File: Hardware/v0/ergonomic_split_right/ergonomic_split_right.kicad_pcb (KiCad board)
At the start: 2 copper layers, 183 x 172.8 mm, 66 parts, among them J2 Left_Interface, SW1 R50, SW10 R31, SW11 R45, SW12 R51, SW13 R02, SW14 R12, SW15 R22, SW16 R32, SW17 R42, SW18 R54, SW19 R03, SW2 R06, SW20 R13, SW21 R23, SW22 R33, SW23 R43, SW24 R53, SW25 R04, SW26 R14, SW27 R24, SW28 R34, SW29 R44, SW3 R16, SW30 R46, SW31 R05, SW32 R15, SW33 R25, SW34 R35, SW35 R55, SW36 R10, SW37 R30, SW39 R00, SW4 R26, SW40 L_Encoder, SW5 R36, SW6 R52, SW7 R01, SW8 R11, SW9 R21, U2 PCAL9555AHF, U9 TCR2EF33

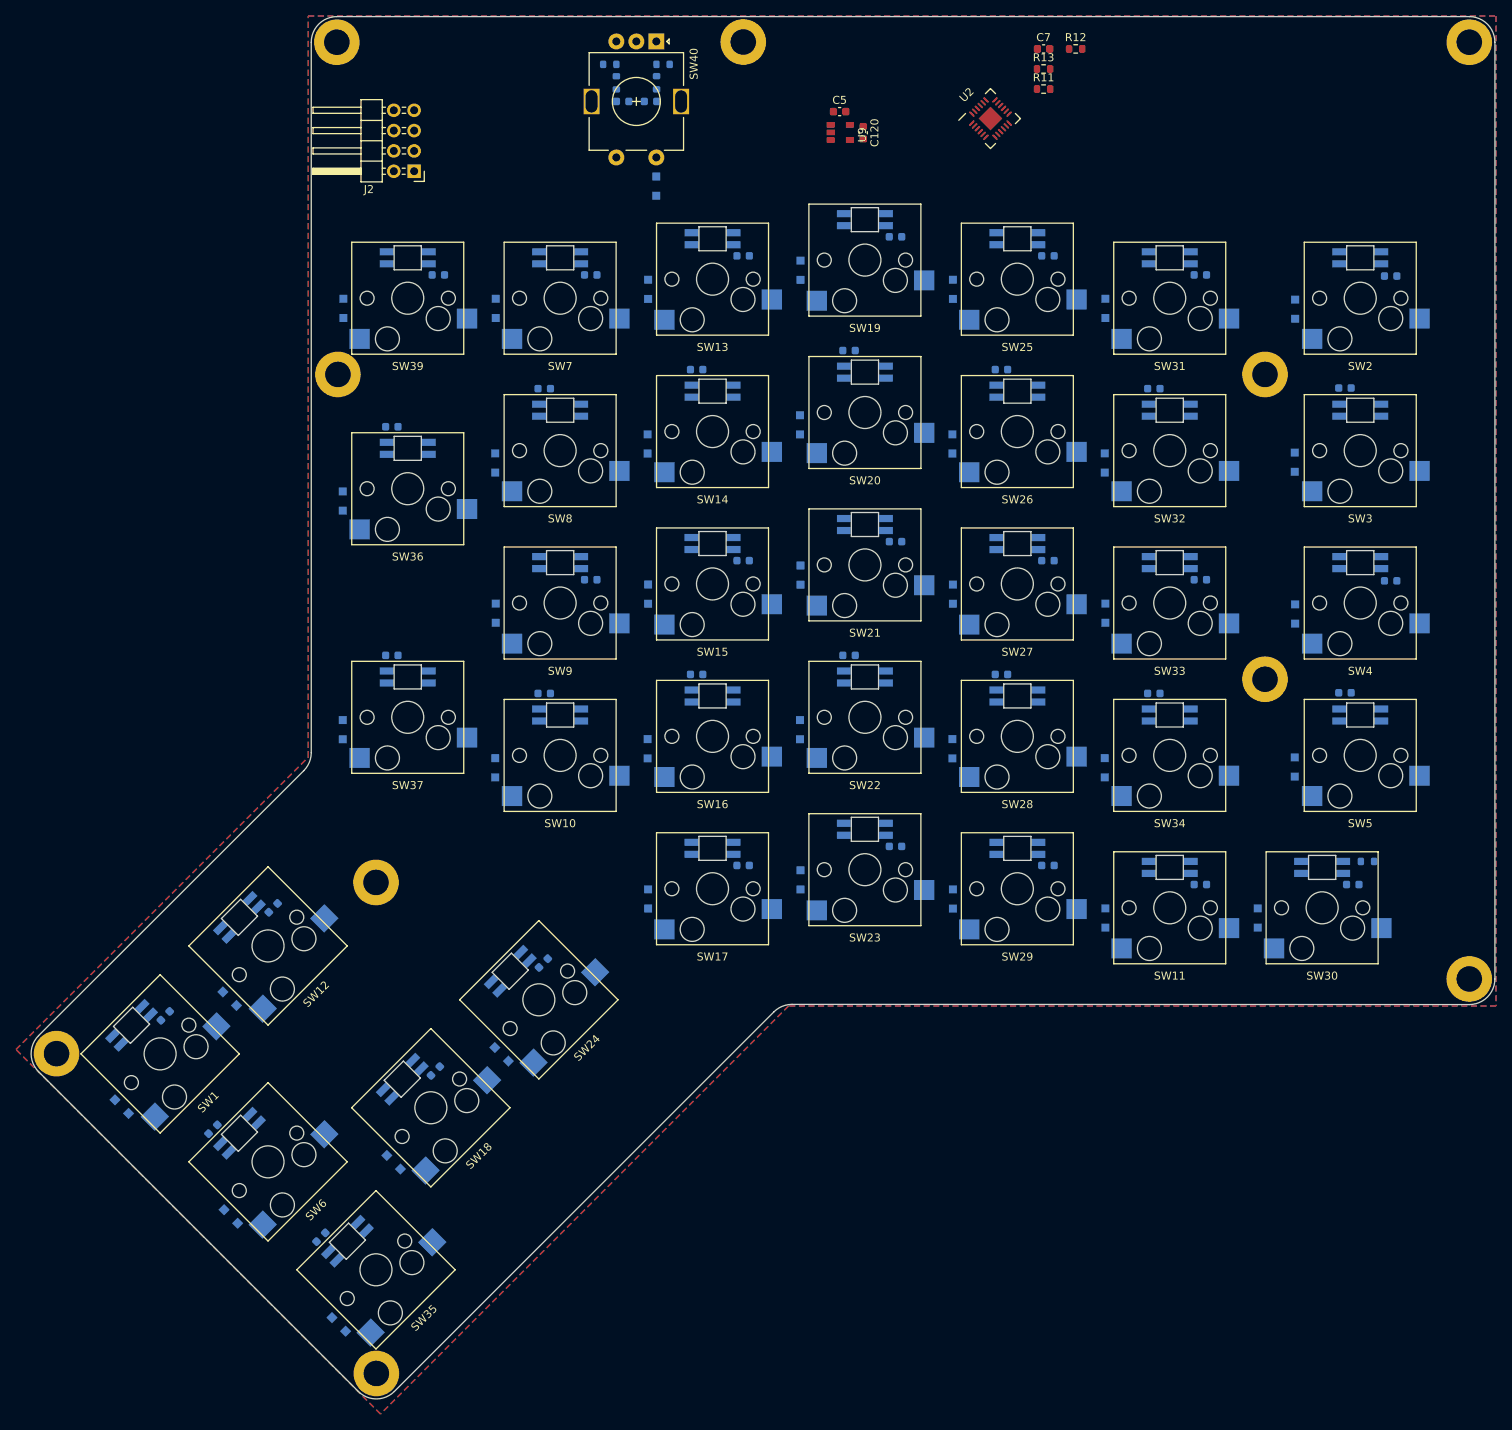
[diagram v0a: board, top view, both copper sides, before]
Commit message: Right side prelim routing mostly done
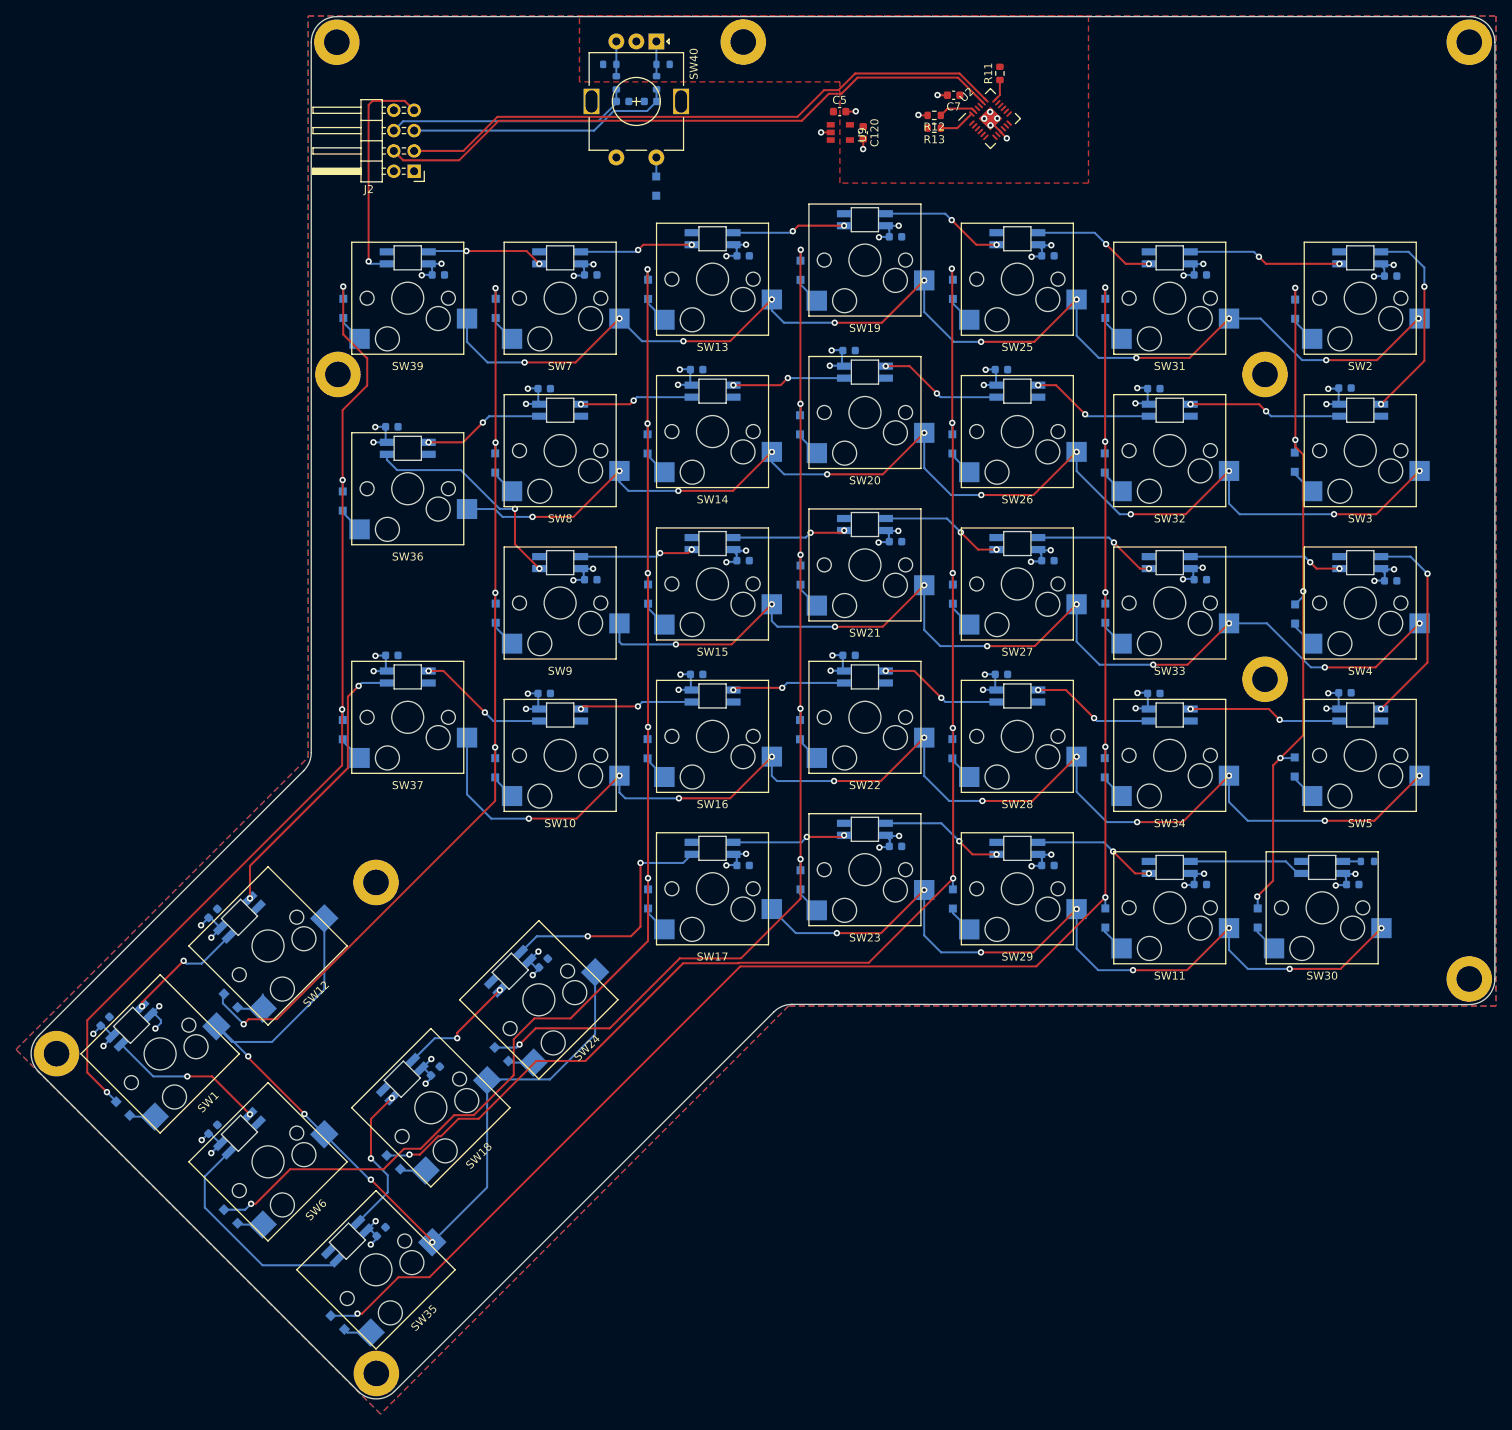
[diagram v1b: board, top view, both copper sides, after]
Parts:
- SW1, SW12: footprint custom_footprint_library:CherryMX_1.00u_KailhSocket_Integrated_Reversed -> custom_footprint_library:CherryMX_1.00u_KailhSocket_Integrated
- SW35: footprint custom_footprint_library:CherryMX_1.00u_KailhSocket_Integrated -> custom_footprint_library:CherryMX_1.00u_KailhSocket_Integrated_Reversed
- SW40: value L_Encoder -> R_Encoder
- moved R12 19.5 mm to (218.2, 50.2), turned to 180 degrees
- moved R13 15.5 mm to (218.2, 51.8), turned to 180 degrees
- moved C7 12.6 mm to (220.6, 47.7), turned to 180 degrees
- moved R11 5.80 mm to (226.4, 44.9), turned to 90 degrees
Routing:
- net /IO Expander/COL[5]: track 0.00 -> 201.8 mm, vias 0 -> 6
- net +5V: track 0.00 -> 175.1 mm, vias 0 -> 76
- net /IO Expander/COL[4]: track 0.00 -> 168.5 mm, vias 0 -> 6
- net /IO Expander/ROW[3]: track 0.00 -> 162.4 mm, vias 0 -> 12
- net /IO Expander/COL[2]: track 0.00 -> 160.6 mm, vias 0 -> 6
- net /IO Expander/ROW[0]: track 0.00 -> 152.4 mm, vias 0 -> 12
- net /IO Expander/ROW[1]: track 0.00 -> 151.5 mm, vias 0 -> 12
- net /IO Expander/COL[3]: track 0.00 -> 134.1 mm, vias 0 -> 6
- net /IO Expander/ROW[2]: track 0.00 -> 130.3 mm, vias 0 -> 10
- net /IO Expander/COL[0]: track 0.00 -> 123.2 mm, vias 0 -> 4
- net /IO Expander/COL[1]: track 0.00 -> 117.6 mm, vias 0 -> 5
- net /IO Expander/ROW[5]: track 0.00 -> 111.0 mm, vias 0 -> 4
- net /IO Expander/ROW[4]: track 0.00 -> 102.5 mm, vias 0 -> 8
- net /IO Expander/COL[6]: track 0.00 -> 87.4 mm, vias 0 -> 5
- net /IO Expander/SCL: track 0.00 -> 79.7 mm
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- added copper zone on F.Cu, net +3V3

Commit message: prelim routing done
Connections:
- D1 pad 1: /IO Expander/COL[6] -> /IO Expander/COL[2]
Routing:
- net /IO Expander/ROW[5]: track 111.0 -> 258.7 mm, vias 4 -> 7
- net /IO Expander/COL[0]: track 123.2 -> 225.4 mm, vias 4 -> 7
- net /IO Expander/ROW[4]: track 102.5 -> 200.6 mm, vias 8 -> 10
- net /IO Expander/COL[1]: track 117.6 -> 203.5 mm, vias 5 -> 8
- net /IO Expander/ROW[3]: track 162.4 -> 242.0 mm, vias 12 -> 14
- net /IO Expander/COL[2]: track 160.6 -> 226.4 mm, vias 6 -> 9
- net /IO Expander/COL[3]: track 134.1 -> 196.7 mm, vias 6 -> 7
- net /IO Expander/ROW[2]: track 130.3 -> 190.1 mm, vias 10 -> 12
- net /IO Expander/ROW[6]: track 0.00 -> 57.8 mm, vias 0 -> 2
- net /IO Expander/COL[6]: track 87.4 -> 140.7 mm, vias 5 -> 6
- net /IO Expander/COL[4]: track 168.5 -> 214.2 mm, vias 6 -> 7
- net /IO Expander/ROW[1]: track 151.5 -> 192.9 mm, vias 12 -> 14
- net /IO Expander/COL[5]: track 201.8 -> 232.9 mm, vias 6 -> 7
- net /IO Expander/ROW[0]: track 152.4 -> 174.7 mm, vias 12 -> 14
- net +3V3: track 0.00 -> 2.36 mm, vias 0 -> 2
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
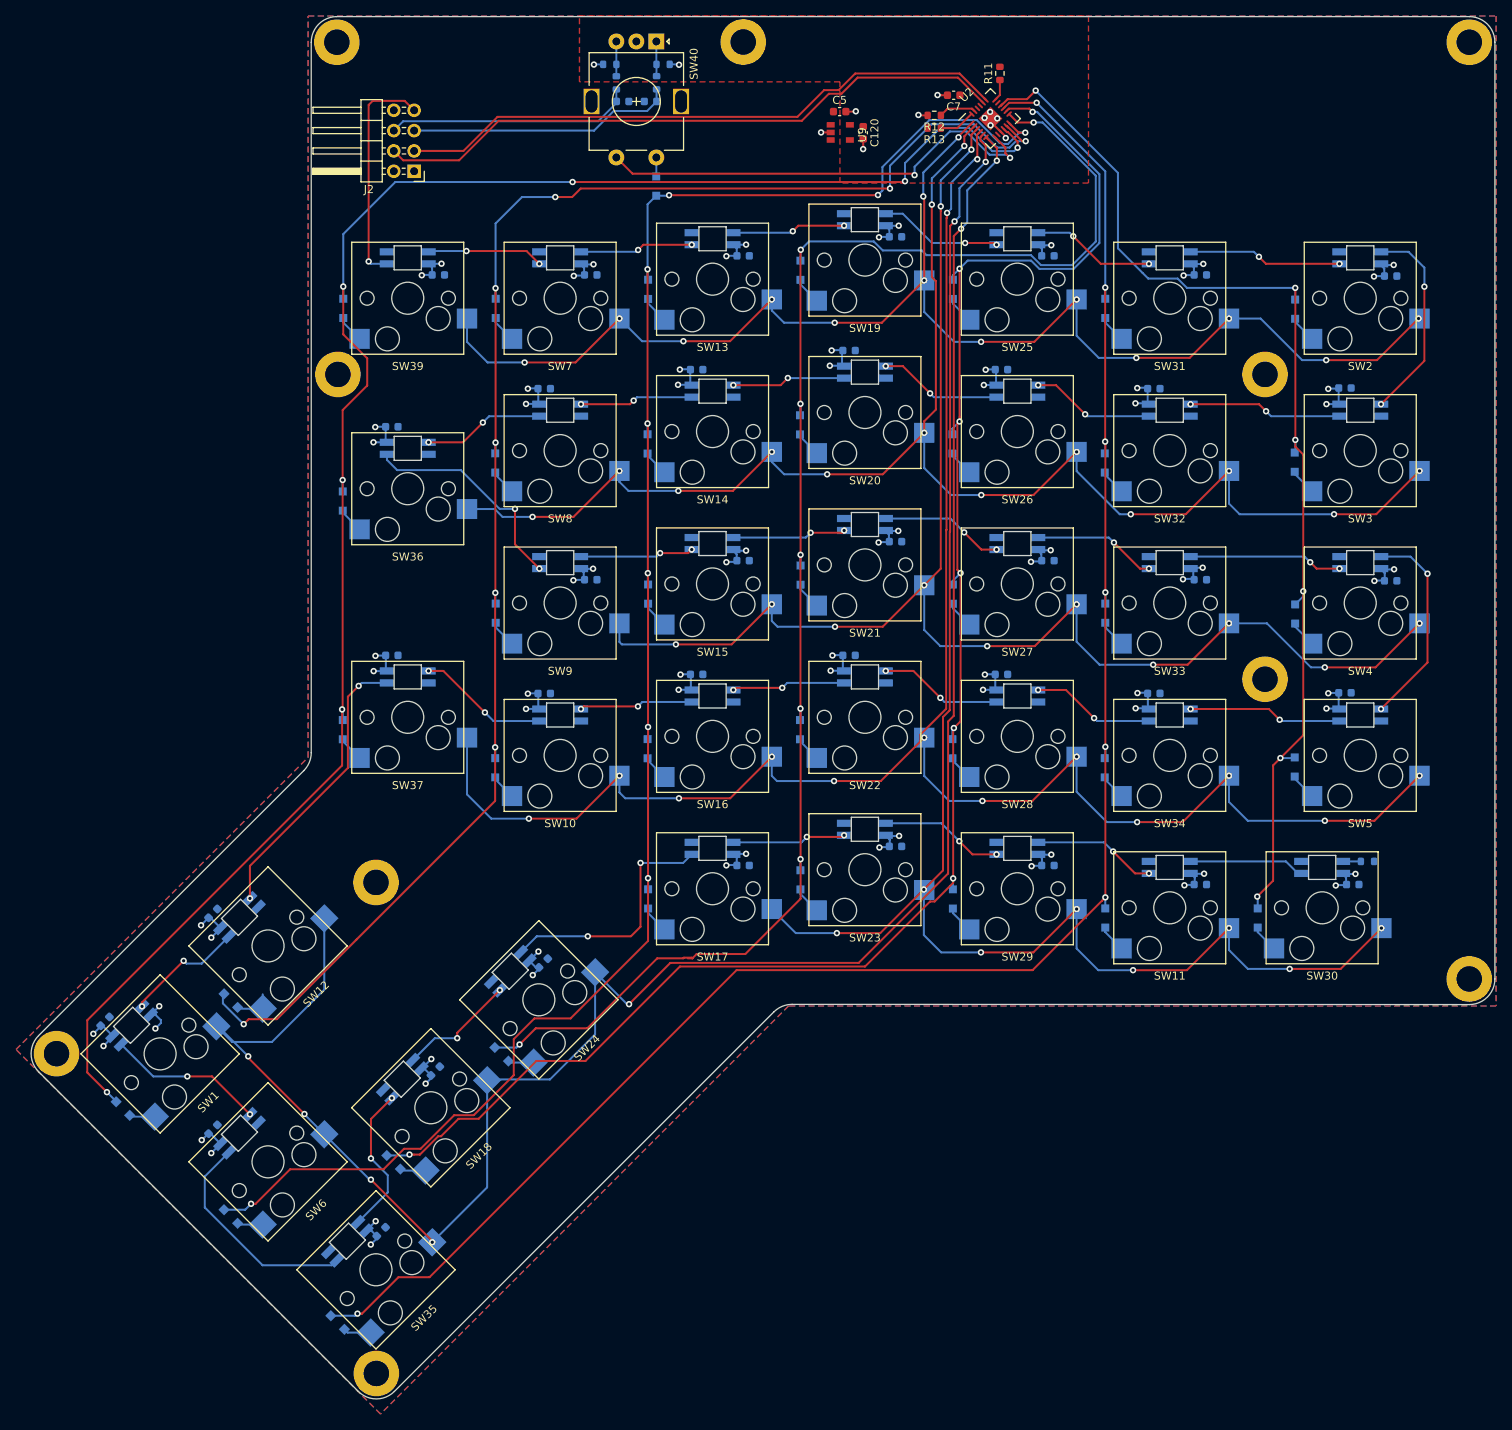
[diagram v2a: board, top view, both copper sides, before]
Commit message: Cleaning routing, fixing 3V3 plane
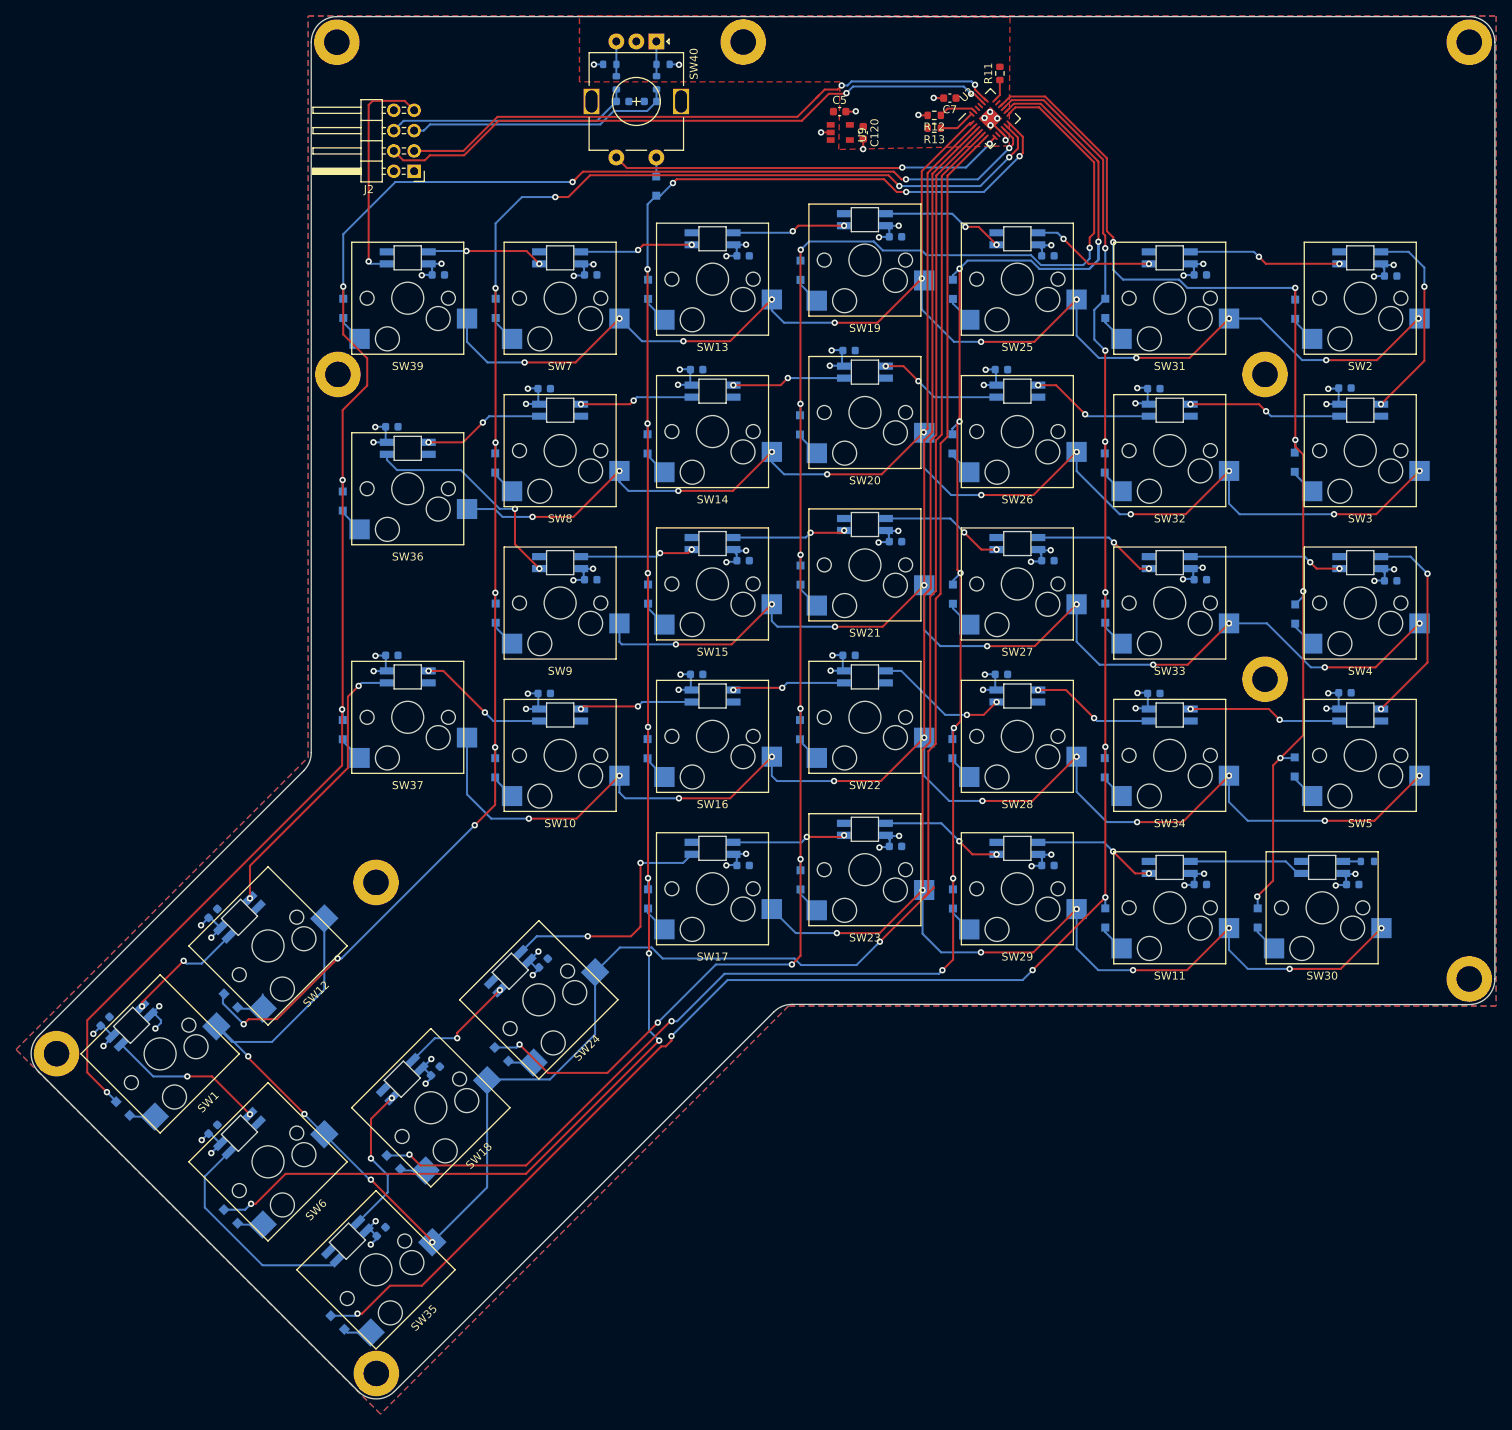
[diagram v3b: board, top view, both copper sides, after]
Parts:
- moved C7 0.60 mm to (220.2, 48.0)
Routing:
- net /IO Expander/COL[4]: track 214.2 -> 231.9 mm, vias 7 -> 9
- net /IO Expander/COL[3]: track 196.7 -> 205.4 mm, vias 7 -> 9
- net /IO Expander/ROW[6]: track 57.8 -> 49.6 mm
- net /IO Expander/COL[2]: track 226.4 -> 232.0 mm, vias 9 -> 11
- net /IO Expander/COL[1]: track 203.5 -> 199.9 mm, vias 8 -> 10
- net /IO Expander/COL[0]: track 225.4 -> 221.9 mm
- net /IO Expander/COL[6]: track 140.7 -> 142.3 mm
- net GND: track 20.9 -> 22.3 mm
- net Net-(SW22-Pad8): track 15.5 -> 16.8 mm
- net /IO Expander/COL[5]: track 232.9 -> 234.0 mm, vias 7 -> 9
- net /IO Expander/SCL: track 79.7 -> 78.8 mm, vias 0 -> 2
- net /IO Expander/ROW[3]: track 242.0 -> 241.1 mm, vias 14 -> 12
- net /IO Expander/ROW[5]: track 258.7 -> 257.9 mm, vias 7 -> 5
- net /IO Expander/ROW[4]: track 200.6 -> 200.0 mm, vias 10 -> 8
- net /IO Expander/ROW[1]: track 192.9 -> 192.5 mm, vias 14 -> 12
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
